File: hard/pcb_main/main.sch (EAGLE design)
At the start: 183 parts

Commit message: nop
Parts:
- added R76: 1kOhm, rcl:R-EU_R0805
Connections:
- new net N$11: D6.4.DA, R76.2
- new net N$54: D6.4.DC, R76.1
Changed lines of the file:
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@@
 <part name="GND36" library="supply" deviceset="GND" device=""/>
 <part name="U$8" library="frame-simplified" deviceset="A2_PORTRAIT_NEXT_SCALED" device=""/>
+<part name="R76" library="rcl" deviceset="R-EU_" device="R0805" value="1kOhm">
+<attribute name="PARTNO" value="ERJ6GEYJ102V"/>
+</part>
 </parts>
 <sheets>
@@
 <instance part="GND36" gate="1" x="99.06" y="58.42"/>
 <instance part="U$8" gate="G$1" x="0" y="0"/>
+<instance part="R76" gate="G$1" x="68.58" y="71.12">
+<attribute name="PARTNO" value="ERJ6GEYJ102V" x="71.12" y="71.12" size="1.778" layer="96" display="off"/>
+</instance>
 </instances>
 <busses>
@@
 </segment>
 </net>
+<net name="N$11" class="0">
+<segment>
+<pinref part="R76" gate="G$1" pin="2"/>
+<pinref part="D6" gate=".4" pin="DA"/>
+<wire x1="73.66" y1="71.12" x2="78.74" y2="71.12" width="0.1524" layer="91"/>
+<wire x1="78.74" y1="71.12" x2="78.74" y2="73.66" width="0.1524" layer="91"/>
+</segment>
+</net>
+<net name="N$54" class="0">
+<segment>
+<pinref part="D6" gate=".4" pin="DC"/>
+<pinref part="R76" gate="G$1" pin="1"/>
+<wire x1="78.74" y1="68.58" x2="63.5" y2="68.58" width="0.1524" layer="91"/>
+<wire x1="63.5" y1="68.58" x2="63.5" y2="71.12" width="0.1524" layer="91"/>
+</segment>
+</net>

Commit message: output schematic improvemetns
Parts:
- added R77, R78, R79, R80, R81, R82, R83: 100Ohm, rcl:R-EU_R0603
- added VD44, VD45, VD46, VD47, VD48, VD49, VD50, VD51, VD52, VD53, VD54, VD55, VD56, VD57, VD58, VD59: (no value), diode:DIODE-STANDARD-SOD323
- R76: value 1kOhm -> 100Ohm; device rcl:R-EU_R0805 -> rcl:R-EU_R0603; PARTNO ERJ6GEYJ102V -> ERJ3GEYJ101V
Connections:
- new net N$55: D6.2.DA, R81.1
- new net N$56: D6.1.DA, R80.1
- new net N$57: D1.4.DA, R79.1
- new net N$58: D1.3.DA, R78.1
- new net N$59: D1.2.DA, R77.1
- new net N$60: D1.1.DA, R76.1
- new net N$62: D2.IFB, VD59.A
- new net N$63: D3.IFB, VD58.A
- new net N$64: D4.IFB, VD57.A
- new net N$65: D5.IFB, VD56.A
- new net N$66: D7.IFB, VD55.A
- new net N$67: D8.IFB, VD54.A
- new net N$68: D9.IFB, VD53.A
- new net N$69: D10.IFB, VD52.A
- net GND: now also D1.1.DC, D1.2.DC, D1.3.DC, D1.4.DC, D6.1.DC, D6.2.DC, D6.3.DC, D6.4.DC, VD44.A, VD45.A, VD46.A, VD47.A, VD48.A, VD49.A, VD50.A, VD51.A, VD52.C, VD53.C, VD54.C, VD55.C, VD56.C, VD57.C, VD58.C, VD59.C; no longer R1.1, R5.1, R6.1, R7.1, R72.1, R73.1, R74.1, R75.1
- net N$1: now also D10.IN, R75.2; no longer D1.1.TC, D2.IN
- net N$10: now also D2.IN; no longer D2.IFB
- net N$11: now also R83.1; no longer R76.2
- net N$3: now also D9.IN, R74.2; no longer D1.2.TC, D3.IN
- net N$4: now also D8.IN, R73.2; no longer D1.3.TC, D4.IN
- net N$46: now also D1.1.TC, R7.1, VD44.C; no longer D6.1.TC, D7.IN
- net N$47: now also D1.2.TC, R1.1, VD45.C; no longer D6.2.TC, D8.IN
- net N$48: now also D1.3.TC, R5.1, VD46.C; no longer D6.3.TC, D9.IN
- net N$49: now also D1.4.TC, R6.1, VD47.C; no longer D10.IN, D6.4.TC
- net N$5: now also D7.IN, R72.2; no longer D1.4.TC, D5.IN
- net N$50: now also D6.1.TC, R72.1, VD48.C; no longer D10.IFB, R75.2
- net N$51: now also D6.2.TC, R73.1, VD49.C; no longer D9.IFB, R74.2
- net N$52: now also D6.3.TC, R74.1, VD50.C; no longer D8.IFB, R73.2
- net N$53: now also D6.4.TC, R75.1, VD51.C; no longer D7.IFB, R72.2
- net N$54: now also D6.3.DA, R82.1; no longer D6.4.DC, R76.1
- net N$6: now also D5.IN; no longer D5.IFB
- net N$8: now also D4.IN; no longer D4.IFB
- net N$9: now also D3.IN; no longer D3.IFB
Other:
- moved on the sheet: D1.1, D1.2, D1.3, D1.4, D10, D2, D3, D4, D5, D6.1, D6.2, D6.3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

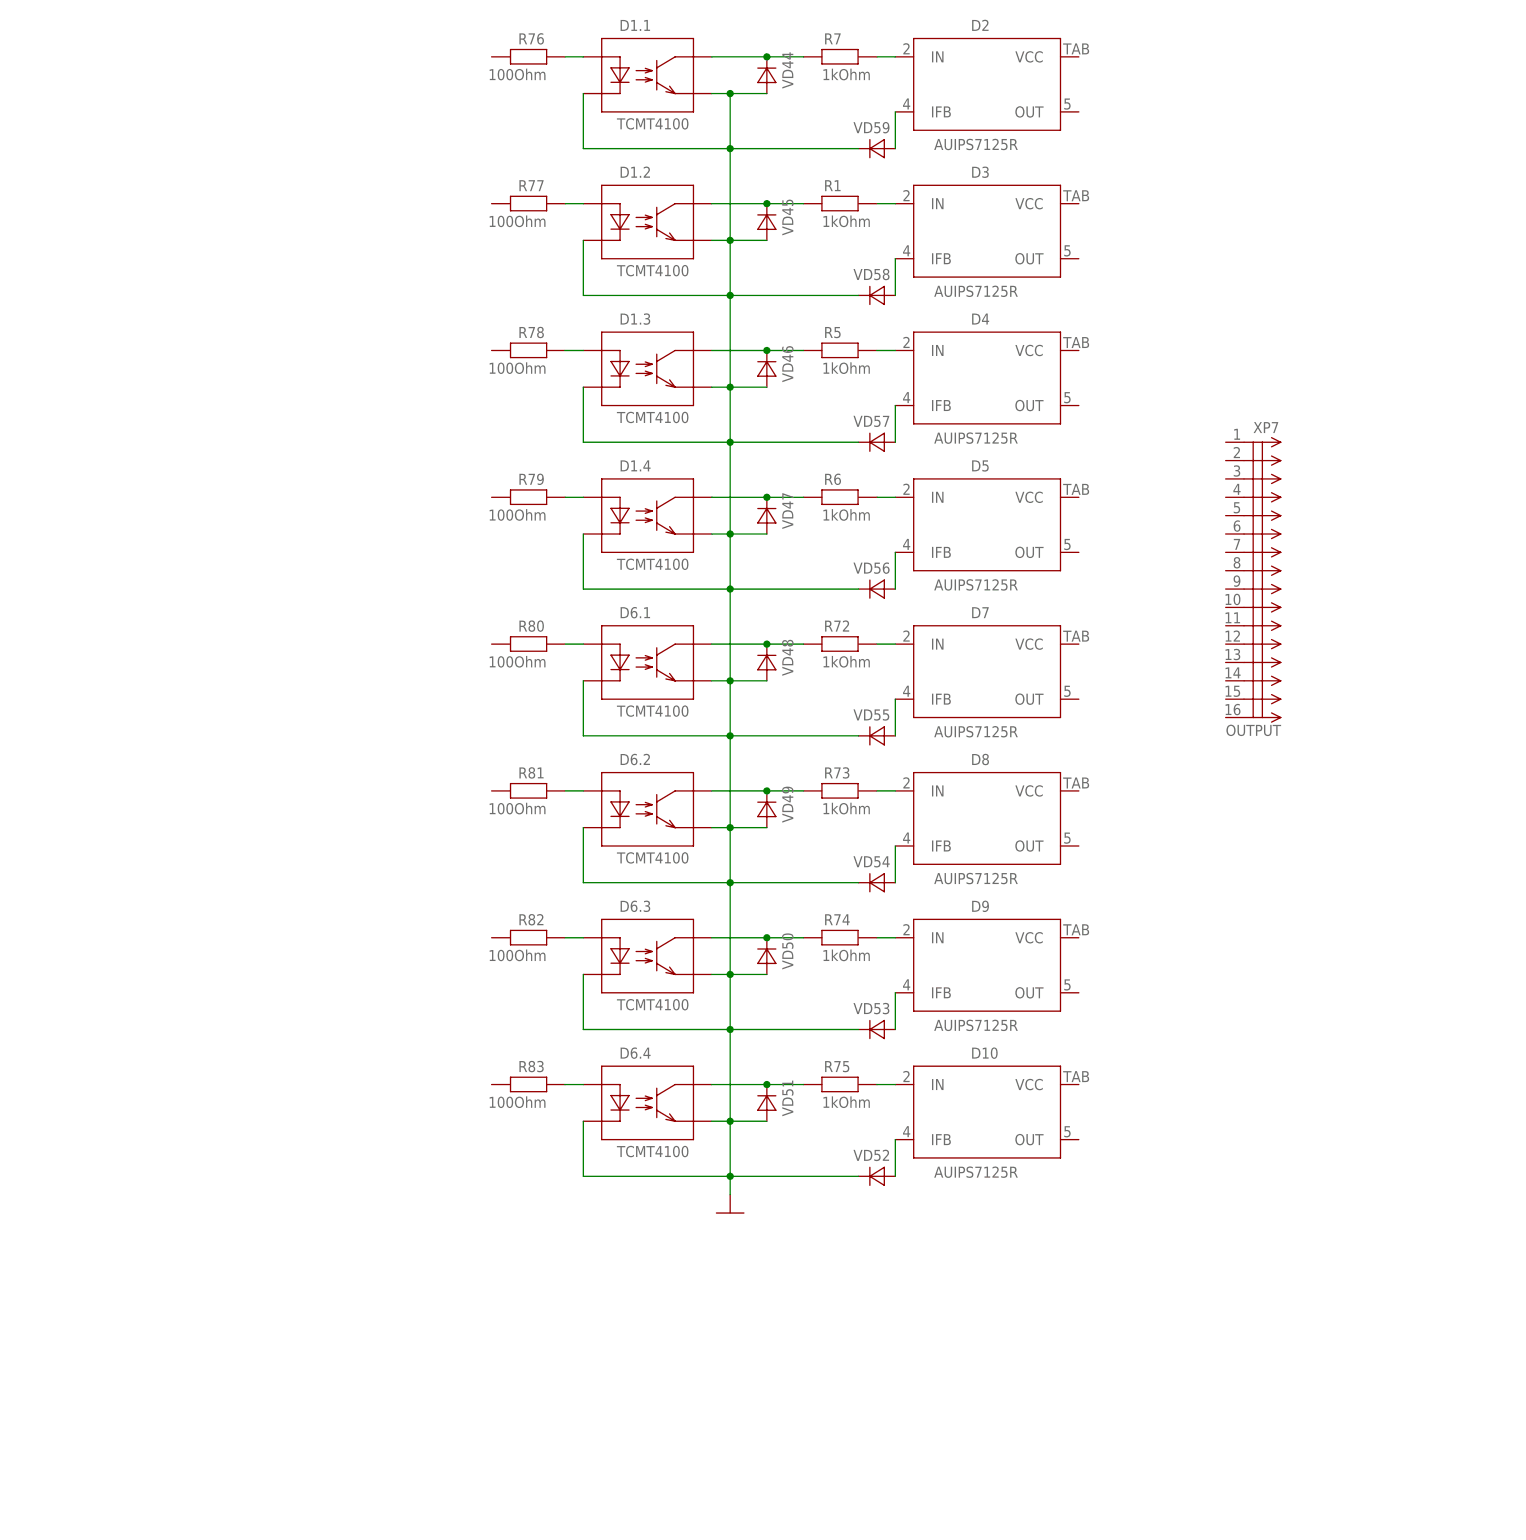
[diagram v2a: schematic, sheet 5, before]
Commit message: added shift register to output block
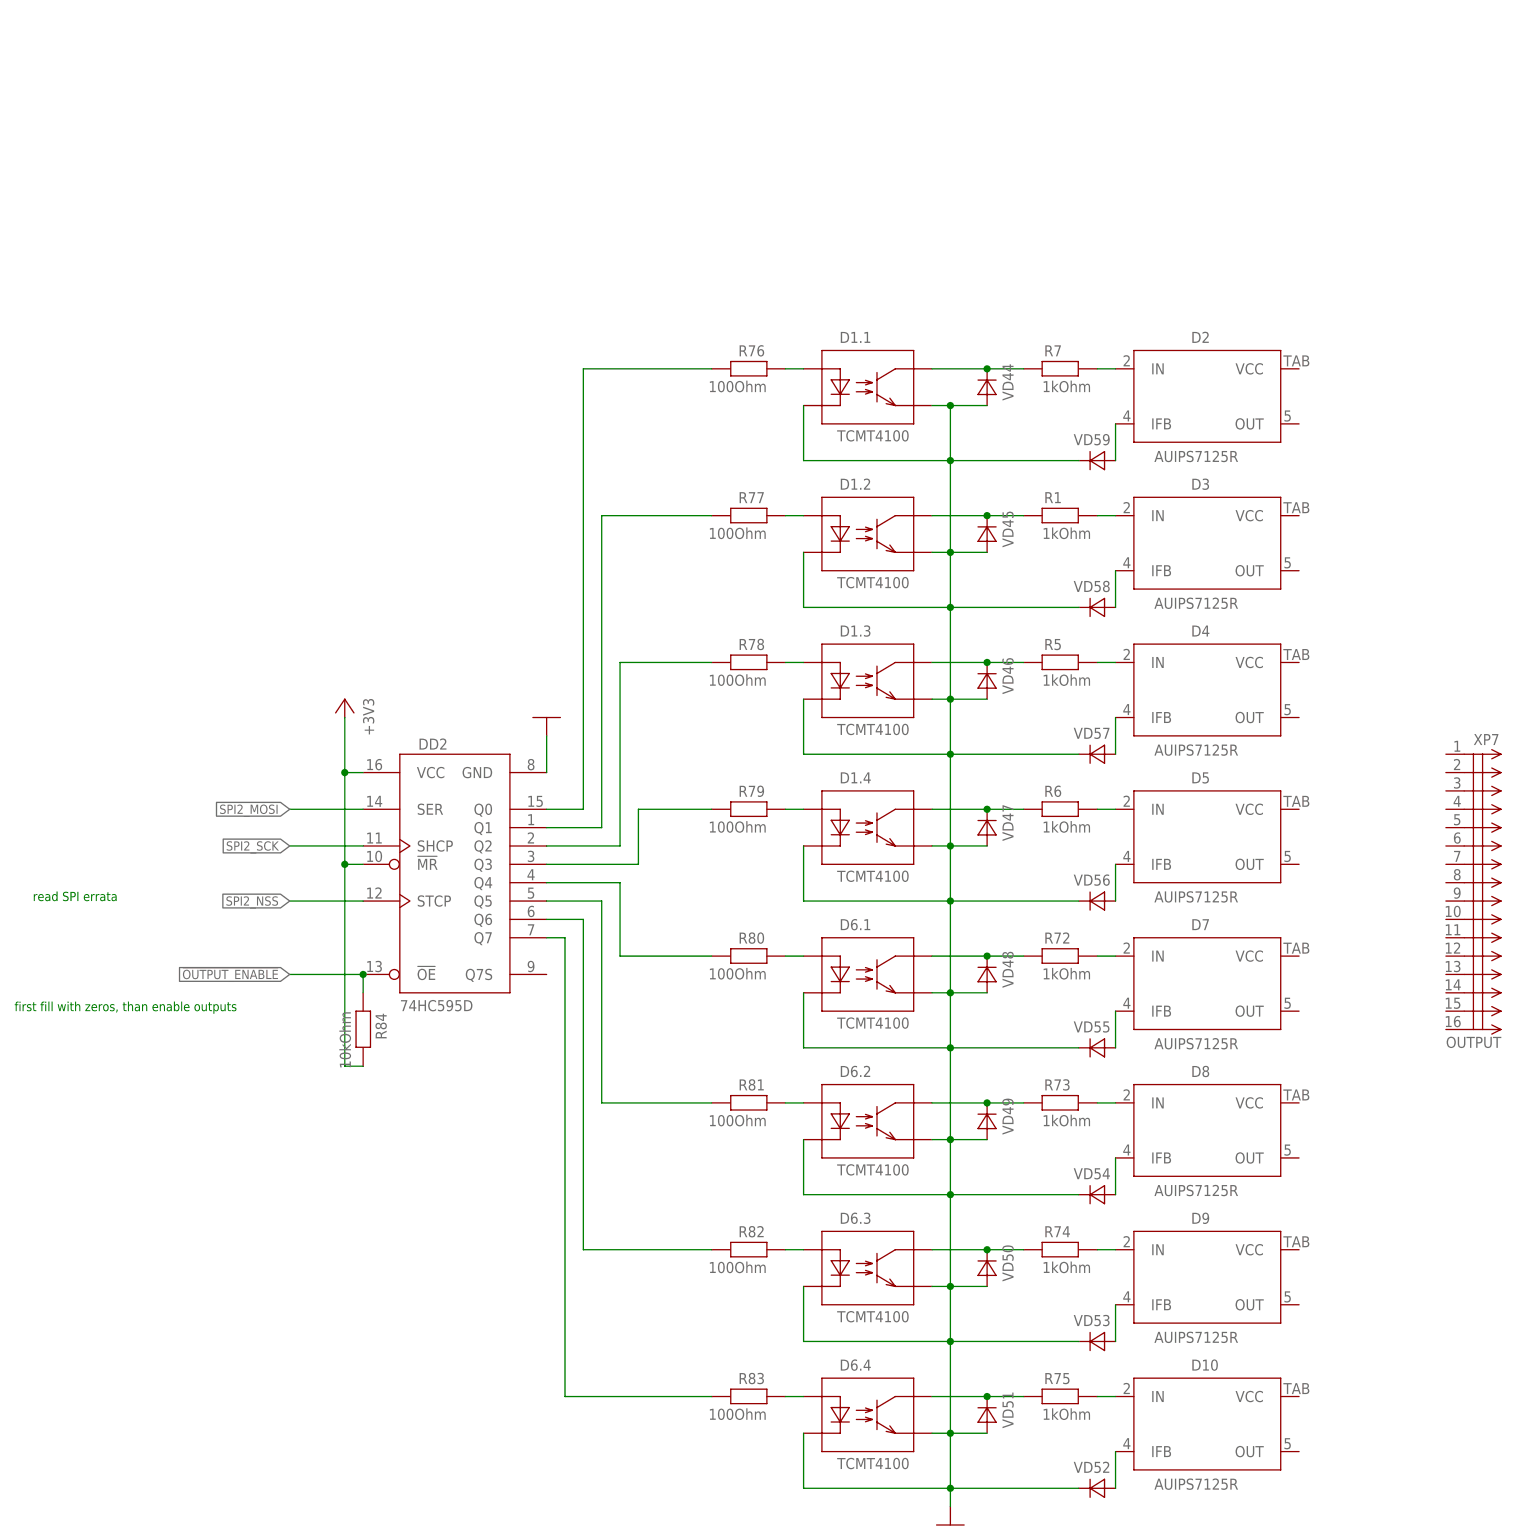
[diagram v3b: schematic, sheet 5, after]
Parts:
- added DD2: 74HC595D, 74xx:74HC595D
- added R84: 10kOhm, rcl:R-EU_R0603
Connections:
- new net !OUTPUT_ENABLE: DD1.PE2(TRACECK/FSMC_A23)*, DD2.!OE, R84.1
- new net N$61: DD2.Q0, R76.2
- new net N$70: DD2.Q1, R77.2
- new net N$71: DD2.Q2, R78.2
- new net N$72: DD2.Q7, R83.2
- new net N$73: DD2.Q6, R82.2
- new net N$74: DD2.Q5, R81.2
- new net N$80: DD2.Q3, R79.2
- new net N$81: DD2.Q4, R80.2
- new net SPI2_MISO: DD1.PB14(SPI2_MISO/USART3_RTS/TIM1_CH2N)*
- new net SPI2_MOSI: DD1.PB15(SPI2_MOSI/I2S2_SD/TIM1_CH3N)*, DD2.SER
- new net SPI2_NSS: DD1.PB12(SPI2_NSS/I2S2_WS/I2C2_SMBA/USART3_CK/TIM1_BKIN)*, DD2.STCP
- new net SPI2_SCK: DD1.PB13(SPI2_SCK/I2S2_SCK/USART3_CTS/TIM1_CH1N)*, DD2.SHCP
- net +3V3: now also DD2.!MR, DD2.VCC, R84.2
- net GND: now also DD2.GND
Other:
- note added: "74HC165"
- note added: "first fill with zeros, than enable outputs"
- note added: "read SPI errata"
- moved on the sheet: D1.1, D1.2, D1.3, D1.4, D10, D2, D3, D4, D5, D6.1, D6.2, D6.3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
